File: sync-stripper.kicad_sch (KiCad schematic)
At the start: 11 parts, among them J1 5V, J2 SYNC, J3 VIDEO, J4 GND, U1 LM1881

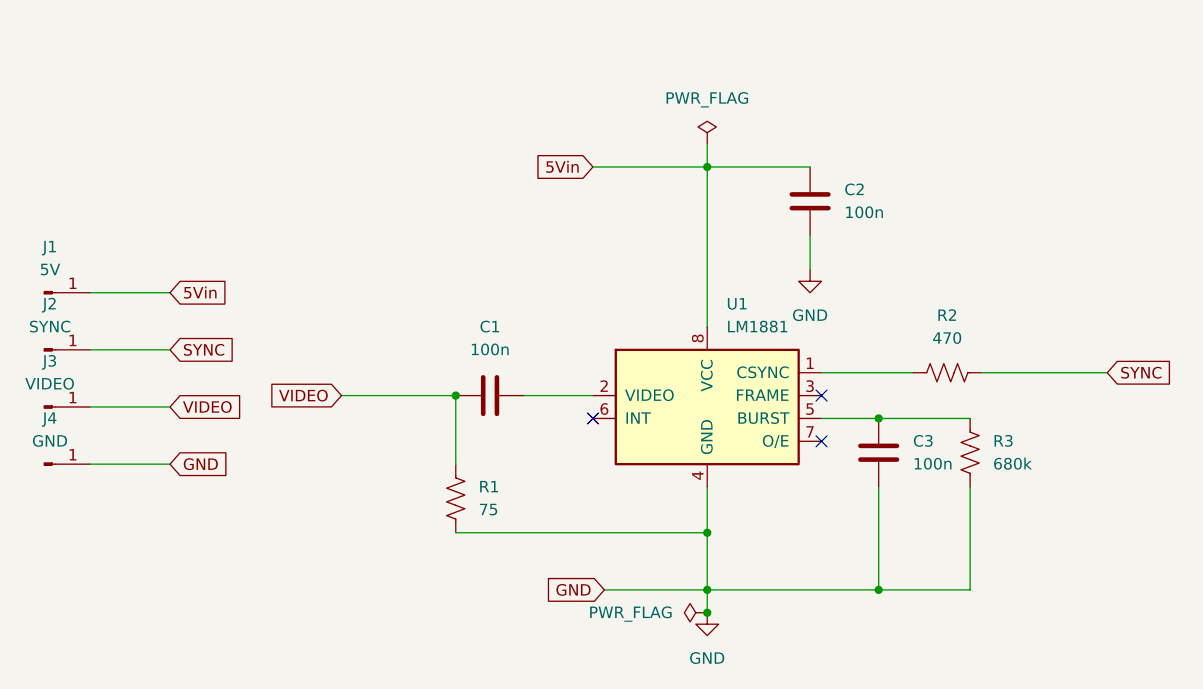
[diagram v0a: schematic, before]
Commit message: Use ground/vcc symbols rather than labels
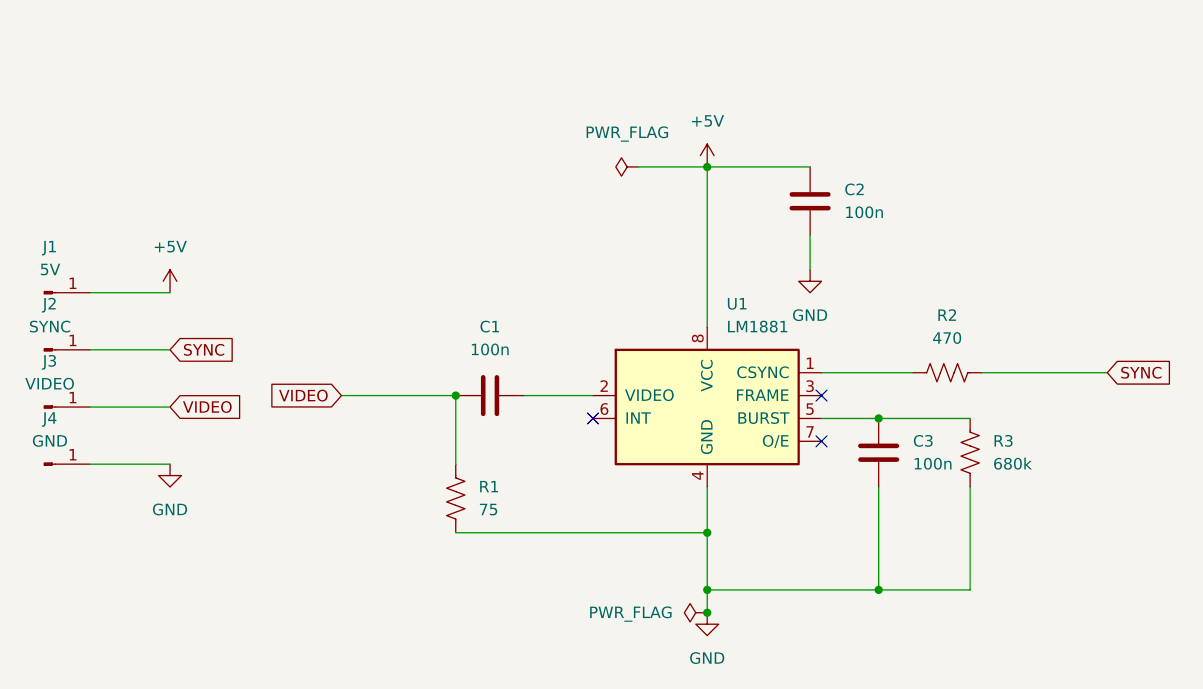
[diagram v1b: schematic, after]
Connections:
- net 5Vin renamed +5V
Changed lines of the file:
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@@
-	(wire
-		(pts
-			(xy 68.58 102.87) (xy 77.47 102.87)
-		)
-		(stroke
-			(width 0)
-			(type default)
-		)
-	)
 	(wire
 		(pts
@@
 	(wire
 		(pts
-			(xy 68.58 83.82) (xy 77.47 83.82)
-		)
-		(stroke
-			(width 0)
-			(type default)
-		)
-	)
-	(wire
-		(pts
 			(xy 156.21 105.41) (xy 156.21 116.84)
 		)
@@
 	(wire
 		(pts
+			(xy 77.47 83.82) (xy 68.58 83.82)
+		)
+		(stroke
+			(width 0)
+			(type default)
+		)
+	)
+	(wire
+		(pts
 			(xy 96.52 95.25) (xy 109.22 95.25)
 		)
@@
 	(wire
 		(pts
+			(xy 77.47 102.87) (xy 68.58 102.87)
+		)
+		(stroke
+			(width 0)
+			(type default)
+		)
+	)
+	(wire
+		(pts
 			(xy 149.86 92.71) (xy 160.02 92.71)
 		)
@@
 	(wire
 		(pts
-			(xy 137.16 67.31) (xy 137.16 69.85)
-		)
-		(stroke
-			(width 0)
-			(type default)
-		)
-	)
-	(wire
-		(pts
-			(xy 125.73 116.84) (xy 137.16 116.84)
-		)
-		(stroke
-			(width 0)
-			(type default)
-		)
-	)
-	(wire
-		(pts
-			(xy 124.46 69.85) (xy 137.16 69.85)
-		)
-		(stroke
-			(width 0)
-			(type default)
-		)
-	)
-	(wire
-		(pts
 			(xy 137.16 116.84) (xy 137.16 119.38)
+		)
+		(stroke
+			(width 0)
+			(type default)
+		)
+	)
+	(wire
+		(pts
+			(xy 129.54 69.85) (xy 137.16 69.85)
 		)
 		(stroke
@@
 		)
 	)
-	(global_label "5Vin"
+	(global_label "VIDEO"
 		(shape input)
-		(at 124.46 69.85 180)
+		(at 77.47 96.52 0)
 		(fields_autoplaced yes)
 		(effects
@@
 				(size 1.27 1.27)
 			)
-			(justify right)
-		)
-		(property "Intersheetrefs" "${INTERSHEET_REFS}"
-			(at 117.4229 69.85 0)
-			(effects
-				(font
-					(size 1.27 1.27)
-				)
-				(justify right)
-				(hide yes)
-			)
-		)
-	)
-	(global_label "5Vin"
-		(shape input)
-		(at 77.47 83.82 0)
-		(fields_autoplaced yes)
-		(effects
-			(font
-				(size 1.27 1.27)
-			)
-			(justify left)
-		)
-		(property "Intersheetrefs" "${INTERSHEET_REFS}"
-			(at 84.5071 83.82 0)
-			(effects
-				(font
-					(size 1.27 1.27)
-				)
-				(justify left)
-				(hide yes)
-			)
-		)
-	)
-	(global_label "GND"
-		(shape input)
-		(at 77.47 102.87 0)
-		(fields_autoplaced yes)
-		(effects
-			(font
-				(size 1.27 1.27)
-			)
-			(justify left)
-		)
-		(property "Intersheetrefs" "${INTERSHEET_REFS}"
-			(at 84.3257 102.87 0)
-			(effects
-				(font
-					(size 1.27 1.27)
-				)
-				(justify left)
-				(hide yes)
-			)
-		)
-	)
-	(global_label "VIDEO"
-		(shape input)
-		(at 77.47 96.52 0)
-		(fields_autoplaced yes)
-		(effects
-			(font
-				(size 1.27 1.27)
-			)
 			(justify left)
 		)
@@
 		)
 	)
-	(global_label "GND"
-		(shape input)
-		(at 125.73 116.84 180)
-		(fields_autoplaced yes)
-		(effects
-			(font
-				(size 1.27 1.27)
-			)
-			(justify right)
-		)
-		(property "Intersheetrefs" "${INTERSHEET_REFS}"
-			(at 118.8743 116.84 0)
-			(effects
-				(font
-					(size 1.27 1.27)
-				)
-				(justify right)
-				(hide yes)
-			)
-		)
-	)
 	(symbol
 		(lib_id "Device:R_US")
@@
 	(symbol
 		(lib_id "power:PWR_FLAG")
-		(at 137.16 67.31 0)
+		(at 129.54 69.85 90)
 		(unit 1)
 		(exclude_from_sim no)
@@
 		(fields_autoplaced yes)
 		(property "Reference" "#FLG01"
-			(at 137.16 65.405 0)
+			(at 127.635 69.85 0)
 			(effects
 				(font
@@
 		)
 		(property "Value" "PWR_FLAG"
-			(at 137.16 62.23 0)
+			(at 128.27 66.04 90)
 			(effects
 				(font
@@
 		)
 		(property "Footprint" ""
-			(at 137.16 67.31 0)
+			(at 129.54 69.85 0)
 			(effects
 				(font
@@
 		)
 		(property "Datasheet" "~"
-			(at 137.16 67.31 0)
+			(at 129.54 69.85 0)
 			(effects
 				(font
@@
 		)
 		(property "Description" "Special symbol for telling ERC where power comes from"
-			(at 137.16 67.31 0)
+			(at 129.54 69.85 0)
 			(effects
 				(font
@@
 	)
 	(symbol
+		(lib_id "power:+5V")
+		(at 137.16 69.85 0)
+		(unit 1)
+		(exclude_from_sim no)
+		(in_bom yes)
+		(on_board yes)
+		(dnp no)
+		(fields_autoplaced yes)
+		(property "Reference" "#PWR05"
+			(at 137.16 73.66 0)
+			(effects
+				(font
+					(size 1.27 1.27)
+				)
+				(hide yes)
+			)
+		)
+		(property "Value" "+5V"
+			(at 137.16 64.77 0)
+			(effects
+				(font
+					(size 1.27 1.27)
+				)
+			)
+		)
+		(property "Footprint" ""
+			(at 137.16 69.85 0)
+			(effects
+				(font
+					(size 1.27 1.27)
+				)
+				(hide yes)
+			)
+		)
+		(property "Datasheet" ""
+			(at 137.16 69.85 0)
+			(effects
+				(font
+					(size 1.27 1.27)
+				)
+				(hide yes)
+			)
+		)
+		(property "Description" "Power symbol creates a global label with name \"+5V\""
+			(at 137.16 69.85 0)
+			(effects
+				(font
+					(size 1.27 1.27)
+				)
+				(hide yes)
+			)
+		)
+		(pin "1"
+		)
+		(instances
+			(project "sync-stripper"
+				(path "/0403b6e4-f433-4bb1-9ddd-10200edbc30d"
+					(reference "#PWR05")
+					(unit 1)
+				)
+			)
+		)
+	)
+	(symbol
 		(lib_id "Video:LM1881")
 		(at 137.16 97.79 0)
@@
 	)
 	(symbol
+		(lib_id "power:GND")
+		(at 77.47 102.87 0)
+		(unit 1)
+		(exclude_from_sim no)
+		(in_bom yes)
+		(on_board yes)
+		(dnp no)
+		(fields_autoplaced yes)
+		(property "Reference" "#PWR01"
+			(at 77.47 109.22 0)
+			(effects
+				(font
+					(size 1.27 1.27)
+				)
+				(hide yes)
+			)
+		)
+		(property "Value" "GND"
+			(at 77.47 107.95 0)
+			(effects
+				(font
+					(size 1.27 1.27)
+				)
+			)
+		)
+		(property "Footprint" ""
+			(at 77.47 102.87 0)
+			(effects
+				(font
+					(size 1.27 1.27)
+				)
+				(hide yes)
+			)
+		)
+		(property "Datasheet" ""
+			(at 77.47 102.87 0)
+			(effects
+				(font
+					(size 1.27 1.27)
+				)
+				(hide yes)
+			)
+		)
+		(property "Description" "Power symbol creates a global label with name \"GND\" , ground"
+			(at 77.47 102.87 0)
+			(effects
+				(font
+					(size 1.27 1.27)
+				)
+				(hide yes)
+			)
+		)
+		(pin "1"
+		)
+		(instances
+			(project ""
+				(path "/0403b6e4-f433-4bb1-9ddd-10200edbc30d"
+					(reference "#PWR01")
+					(unit 1)
+				)
+			)
+		)
+	)
+	(symbol
 		(lib_id "Connector:Conn_01x01_Pin")
 		(at 63.5 83.82 0)
@@
 					(unit 1)
 				)
+			)
+		)
+	)
+	(symbol
+		(lib_id "power:+5V")
+		(at 77.47 83.82 0)
+		(unit 1)
+		(exclude_from_sim no)
+		(in_bom yes)
+		(on_board yes)
+		(dnp no)
+		(fields_autoplaced yes)
+		(property "Reference" "#PWR04"
+			(at 77.47 87.63 0)
+			(effects
+				(font
+					(size 1.27 1.27)
+				)
+				(hide yes)
+			)
+		)
+		(property "Value" "+5V"
+			(at 77.47 78.74 0)
+			(effects
+				(font
+					(size 1.27 1.27)
+				)
+			)
+		)
+		(property "Footprint" ""
+			(at 77.47 83.82 0)
+			(effects
+				(font
+					(size 1.27 1.27)
+				)
+				(hide yes)
+			)
+		)
+		(property "Datasheet" ""
+			(at 77.47 83.82 0)
+			(effects
+				(font
+					(size 1.27 1.27)
+				)
+				(hide yes)
+			)
+		)
+		(property "Description" "Power symbol creates a global label with name \"+5V\""
+			(at 77.47 83.82 0)
+			(effects
+				(font
+					(size 1.27 1.27)
+				)
+				(hide yes)
+			)
+		)
+		(pin "1"
+		)
+		(instances
+			(project ""
+				(path "/0403b6e4-f433-4bb1-9ddd-10200edbc30d"
+					(reference "#PWR04")
+					(unit 1)
+				)

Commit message: More compact design
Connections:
- net SYNC: no longer names the net of J2.1 (Pin_1), R2.2
- net VIDEO: no longer names the net of C1.2, J3.1 (Pin_1), R1.1
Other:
- moved on the sheet: J1, J2, J3, J4

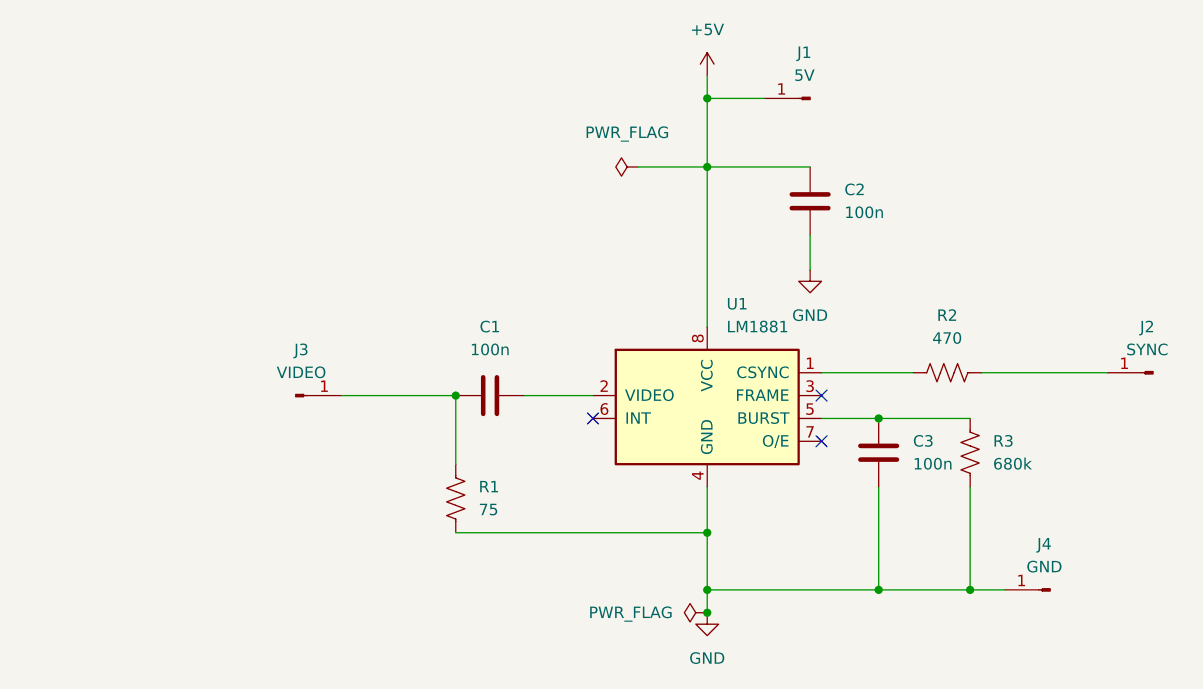
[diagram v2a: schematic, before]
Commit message: Remove KiCad BOM, remove Rset usage, add second ground plane and ground vias
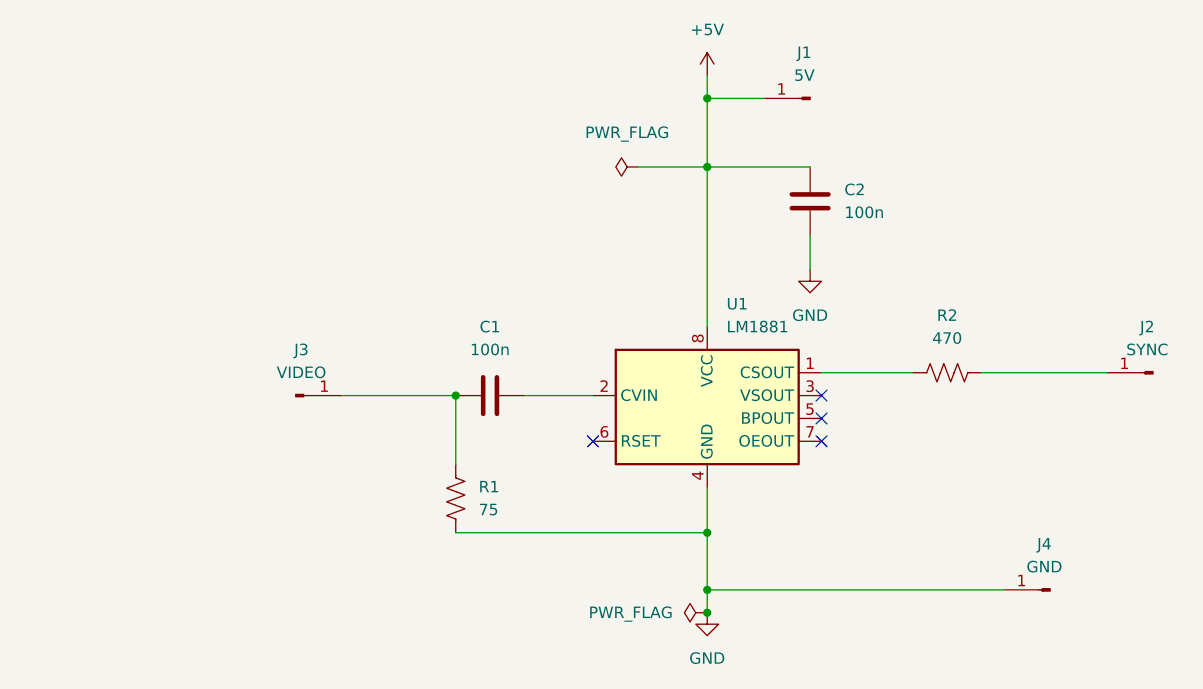
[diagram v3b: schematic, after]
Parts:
- removed C3: 100n, Capacitor_SMD:C_0603_1608Metric_Pad1.08x0.95mm_HandSolder, symbol Device:C
- removed R3: 680k, Resistor_SMD:R_0603_1608Metric_Pad0.98x0.95mm_HandSolder, symbol Device:R_US
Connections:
- no-connect marks 3 -> 4
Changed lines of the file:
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@@
-	)
-	(junction
-		(at 156.21 116.84)
-		(diameter 0)
-		(color 0 0 0 0)
-	)
-	(junction
-		(at 156.21 97.79)
-		(diameter 0)
-		(color 0 0 0 0)
 	)
 	(junction
@@
 		(color 0 0 0 0)
 	)
-	(junction
-		(at 166.37 116.84)
-		(diameter 0)
-		(color 0 0 0 0)
+	(no_connect
+		(at 149.86 97.79)
 	)
 	(no_connect
@@
 	)
 	(no_connect
-		(at 124.46 97.79)
+		(at 124.46 100.33)
 	)
 	(wire
@@
 	(wire
 		(pts
-			(xy 166.37 105.41) (xy 166.37 116.84)
-		)
-		(stroke
-			(width 0)
-			(type default)
-		)
-	)
-	(wire
-		(pts
-			(xy 156.21 105.41) (xy 156.21 116.84)
-		)
-		(stroke
-			(width 0)
-			(type default)
-		)
-	)
-	(wire
-		(pts
-			(xy 156.21 97.79) (xy 166.37 97.79)
-		)
-		(stroke
-			(width 0)
-			(type default)
-		)
-	)
-	(wire
-		(pts
 			(xy 96.52 95.25) (xy 109.22 95.25)
 		)
@@
 	(wire
 		(pts
-			(xy 170.18 116.84) (xy 166.37 116.84)
-		)
-		(stroke
-			(width 0)
-			(type default)
-		)
-	)
-	(wire
-		(pts
-			(xy 156.21 116.84) (xy 137.16 116.84)
+			(xy 137.16 116.84) (xy 170.18 116.84)
 		)
 		(stroke
@@
 	(wire
 		(pts
-			(xy 149.86 97.79) (xy 156.21 97.79)
-		)
-		(stroke
-			(width 0)
-			(type default)
-		)
-	)
-	(wire
-		(pts
 			(xy 116.84 95.25) (xy 124.46 95.25)
 		)
@@
 		(pts
 			(xy 149.86 92.71) (xy 160.02 92.71)
-		)
-		(stroke
-			(width 0)
-			(type default)
-		)
-	)
-	(wire
-		(pts
-			(xy 166.37 116.84) (xy 156.21 116.84)
 		)
 		(stroke
@@
 	)
 	(symbol
-		(lib_id "Device:R_US")
-		(at 166.37 101.6 0)
-		(unit 1)
-		(exclude_from_sim no)
-		(in_bom yes)
-		(on_board yes)
-		(dnp no)
-		(fields_autoplaced yes)
-		(property "Reference" "R3"
-			(at 168.91 100.3299 0)
-			(effects
-				(font
-					(size 1.27 1.27)
-				)
-				(justify left)
-			)
-		)
-		(property "Value" "680k"
-			(at 168.91 102.8699 0)
-			(effects
-				(font
-					(size 1.27 1.27)
-				)
-				(justify left)
-			)
-		)
-		(property "Footprint" "Resistor_SMD:R_0603_1608Metric_Pad0.98x0.95mm_HandSolder"
-			(at 167.386 101.854 90)
-			(effects
-				(font
-					(size 1.27 1.27)
-				)
-				(hide yes)
-			)
-		)
-		(property "Datasheet" "~"
-			(at 166.37 101.6 0)
-			(effects
-				(font
-					(size 1.27 1.27)
-				)
-				(hide yes)
-			)
-		)
-		(property "Description" "Resistor, US symbol"
-			(at 166.37 101.6 0)
-			(effects
-				(font
-					(size 1.27 1.27)
-				)
-				(hide yes)
-			)
-		)
-		(pin "2"
-		)
-		(pin "1"
-		)
-		(instances
-			(project ""
-				(path "/0403b6e4-f433-4bb1-9ddd-10200edbc30d"
-					(reference "R3")
-					(unit 1)
-				)
-			)
-		)
-	)
-	(symbol
 		(lib_id "power:PWR_FLAG")
 		(at 129.54 69.85 90)
@@
 	)
 	(symbol
-		(lib_id "Video:LM1881")
-		(at 137.16 97.79 0)
-		(unit 1)
-		(exclude_from_sim no)
-		(in_bom yes)
-		(on_board yes)
-		(dnp no)
-		(fields_autoplaced yes)
-		(property "Reference" "U1"
-			(at 139.3033 85.09 0)
-			(effects
-				(font
-					(size 1.27 1.27)
-				)
-				(justify left)
-			)
-		)
-		(property "Value" "LM1881"
-			(at 139.3033 87.63 0)
-			(effects
-				(font
-					(size 1.27 1.27)
-				)
-				(justify left)
-			)
-		)
-		(property "Footprint" "Package_SO:SOIC-8_3.9x4.9mm_P1.27mm"
-			(at 137.16 97.79 0)
-			(effects
-				(font
-					(size 1.27 1.27)
-				)
-				(hide yes)
-			)
-		)
-		(property "Datasheet" ""
-			(at 137.16 97.79 0)
-			(effects
-				(font
-					(size 1.27 1.27)
-				)
-				(hide yes)
-			)
-		)
-		(property "Description" ""
-			(at 137.16 97.79 0)
-			(effects
-				(font
-					(size 1.27 1.27)
-				)
-				(hide yes)
-			)
-		)
-		(pin "7"
-		)
-		(pin "5"
-		)
-		(pin "1"
-		)
-		(pin "6"
-		)
-		(pin "2"
-		)
-		(pin "8"
-		)
-		(pin "3"
-		)
-		(pin "4"
-		)
-		(instances
-			(project ""
-				(path "/0403b6e4-f433-4bb1-9ddd-10200edbc30d"
-					(reference "U1")
-					(unit 1)
-				)
-			)
-		)
-	)
-	(symbol
 		(lib_id "Connector:Conn_01x01_Pin")
 		(at 175.26 116.84 180)
@@
 	)
 	(symbol
-		(lib_id "Device:C")
-		(at 156.21 101.6 0)
+		(lib_id "Video:LM1881")
+		(at 137.16 97.79 0)
 		(unit 1)
 		(exclude_from_sim no)
@@
 		(dnp no)
 		(fields_autoplaced yes)
-		(property "Reference" "C3"
-			(at 160.02 100.3299 0)
+		(property "Reference" "U1"
+			(at 139.3033 85.09 0)
 			(effects
 				(font
@@
 			)
 		)
-		(property "Value" "100n"
-			(at 160.02 102.8699 0)
+		(property "Value" "LM1881"
+			(at 139.3033 87.63 0)
 			(effects
 				(font
@@
 			)
 		)
-		(property "Footprint" "Capacitor_SMD:C_0603_1608Metric_Pad1.08x0.95mm_HandSolder"
-			(at 157.1752 105.41 0)
-			(effects
-				(font
-					(size 1.27 1.27)
-				)
-				(hide yes)
-			)
-		)
-		(property "Datasheet" "~"
-			(at 156.21 101.6 0)
-			(effects
-				(font
-					(size 1.27 1.27)
-				)
-				(hide yes)
-			)
-		)
-		(property "Description" "Unpolarized capacitor"
-			(at 156.21 101.6 0)
-			(effects
-				(font
-					(size 1.27 1.27)
-				)
-				(hide yes)
-			)
+		(property "Footprint" "Package_SO:SOIC-8_3.9x4.9mm_P1.27mm"
+			(at 137.16 113.792 0)
+			(effects
+				(font
+					(size 1.27 1.27)
+				)
+				(hide yes)
+			)
+		)
+		(property "Datasheet" "https://www.ti.com/lit/ds/symlink/lm1881.pdf"
+			(at 137.16 111.506 0)
+			(effects
+				(font
+					(size 1.27 1.27)
+				)
+				(hide yes)
+			)
+		)
+		(property "Description" "Video Sync Separator, composite sync and vertical sync outputs, DIP-8 / SOIC-8"
+			(at 137.16 109.22 0)
+			(effects
+				(font
+					(size 1.27 1.27)
+				)
+				(hide yes)
+			)
+		)
+		(pin "2"
+		)
+		(pin "7"
+		)
+		(pin "6"
+		)
+		(pin "5"
+		)
+		(pin "3"
 		)
 		(pin "1"
 		)
-		(pin "2"
+		(pin "4"
+		)
+		(pin "8"
 		)
 		(instances
 			(project ""
 				(path "/0403b6e4-f433-4bb1-9ddd-10200edbc30d"
-					(reference "C3")
+					(reference "U1")
 					(unit 1)
 				)
